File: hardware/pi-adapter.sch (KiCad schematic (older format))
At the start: 31 parts, among them P1 CONN_02X20, P10 CONN_01X04, P11 CONN_01X04, P12 CONN_01X04, P13 CONN_01X04, P14 CONN_01X04, P15 CONN_01X04, P16 CONN_01X04, P17 CONN_01X04, P18 CONN_01X04, P19 CONN_01X04, P2 +5V, P20 CONN_01X04, P21 CONN_01X04, P3 CONN_01X03, P4 GND, P5 CONN_01X03, P6 CONN_01X04, P7 CONN_01X04, P8 CONN_01X04, P9 CONN_01X04, U1 74HCT245, U2 74HCT245, U3 74HCT245, U4 74HCT245

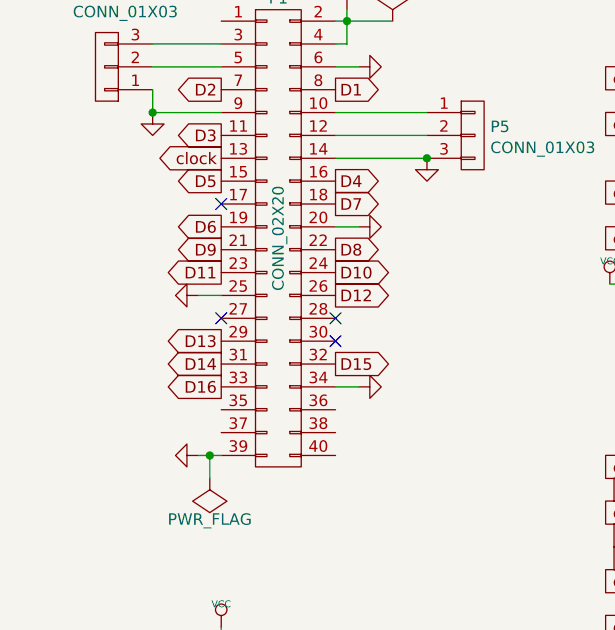
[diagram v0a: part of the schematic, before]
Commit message: o Break out SPI bus as well.
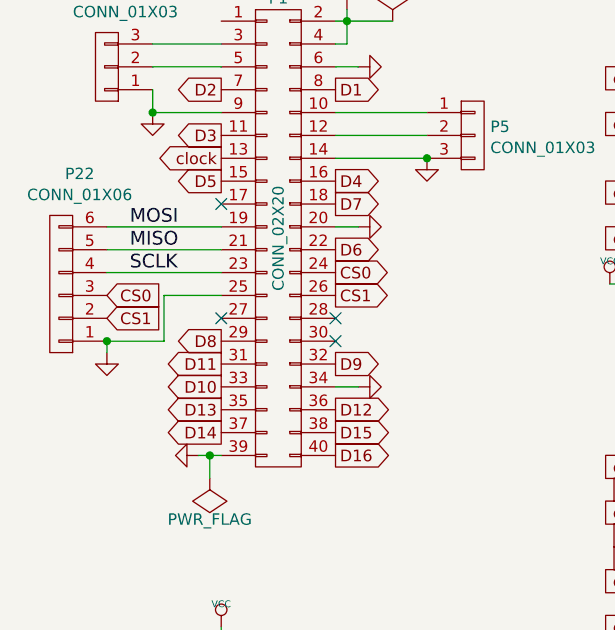
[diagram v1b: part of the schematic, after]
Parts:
- added P22: CONN_01X06, Pin_Headers:Pin_Header_Straight_1x06, symbol CONN_01X06
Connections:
- net D10: now also P1.33 (P33); no longer P1.24 (P24)
- net D11: now also P1.31 (P31); no longer P1.23 (P23)
- net D12: now also P1.36 (P36); no longer P1.26 (P26)
- net D13: now also P1.35 (P35); no longer P1.29 (P29)
- net D14: now also P1.37 (P37); no longer P1.31 (P31)
- net D15: now also P1.38 (P38); no longer P1.32 (P32)
- net D16: now also P1.40 (P40); no longer P1.33 (P33)
- net D6: now also P1.22 (P22); no longer P1.19 (P19)
- net D8: now also P1.29 (P29); no longer P1.22 (P22)
- net D9: now also P1.32 (P32); no longer P1.21 (P21)
- net GND: now also P22.1 (P1)
- new net CS0: P1.24 (P24), P22.3 (P3)
- new net CS1: P1.26 (P26), P22.2 (P2)
- new net MISO: P1.21 (P21), P22.5 (P5)
- new net MOSI: P1.19 (P19), P22.6 (P6)
- new net SCLK: P1.23 (P23), P22.4 (P4)
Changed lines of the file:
@@
 L GND #PWR05
 U 1 1 54ECB7BC
-P 1800 3900
-F 0 "#PWR05" H 1800 3900 30  0001 C CNN
-F 1 "GND" H 1800 3830 30  0001 C CNN
-F 2 "" H 1800 3900 60  0000 C CNN
-F 3 "" H 1800 3900 60  0000 C CNN
-	1    1800 3900
-	0    1    1    0
-$EndComp
-Wire Wire Line
-	1800 3900 1900 3900
+P 1400 4150
+F 0 "#PWR05" H 1400 4150 30  0001 C CNN
+F 1 "GND" H 1400 4080 30  0001 C CNN
+F 2 "" H 1400 4150 60  0000 C CNN
+F 3 "" H 1400 4150 60  0000 C CNN
+	1    1400 4150
+	1    0    0    -1
+$EndComp
+Wire Wire Line
+	1650 3900 1900 3900
 Text GLabel 1900 3000 0    51   Output ~ 0
 D2
-Text GLabel 2400 3700 2    51   Output ~ 0
+Text GLabel 1900 4100 0    51   Output ~ 0
 D8
-Text GLabel 1900 3700 0    51   Output ~ 0
+Text GLabel 2400 4200 2    51   Output ~ 0
 D9
-Text GLabel 2400 3800 2    51   Output ~ 0
+Text GLabel 1900 4300 0    51   Output ~ 0
 D10
-Text GLabel 1900 4100 0    51   Output ~ 0
+Text GLabel 1900 4400 0    51   Output ~ 0
 D13
 Text GLabel 1900 3300 0    51   Output ~ 0
 clock
+Text GLabel 1900 4500 0    51   Output ~ 0
+D14
+Text GLabel 2400 3700 2    51   Output ~ 0
+D6
+Text GLabel 2400 4600 2    51   Output ~ 0
+D16
+Text GLabel 2400 4500 2    51   Output ~ 0
+D15
+Text GLabel 2400 4400 2    51   Output ~ 0
+D12
 Text GLabel 1900 4200 0    51   Output ~ 0
-D14
-Text GLabel 1900 3600 0    51   Output ~ 0
-D6
-Text GLabel 1900 4300 0    51   Output ~ 0
-D16
-Text GLabel 2400 4200 2    51   Output ~ 0
-D15
-Text GLabel 2400 3900 2    51   Output ~ 0
-D12
-Text GLabel 1900 3800 0    51   Output ~ 0
 D11
 Text GLabel 1900 3400 0    51   Output ~ 0
@@
 Text Notes 5150 6100 0    60   ~ 0
 GND CLK DO +5V\n
+Wire Wire Line
+	1400 3600 1900 3600
+Wire Wire Line
+	1400 3700 1900 3700
+Wire Wire Line
+	1400 3800 1900 3800
+$Comp
+L CONN_01X06 P22
+U 1 1 56C265D6
+P 1200 3850
+F 0 "P22" H 1119 3368 50  0000 C CNN
+F 1 "CONN_01X06" H 1119 3460 50  0000 C CNN
+F 2 "Pin_Headers:Pin_Header_Straight_1x06" H 1119 3460 50  0001 C CNN
+F 3 "" H 1200 3850 50  0000 C CNN
+	1    1200 3850
+	-1   0    0    1
+$EndComp
+Wire Wire Line
+	1400 4100 1400 4150
+Wire Wire Line
+	1400 4100 1650 4100
+Wire Wire Line
+	1650 4100 1650 3900
+Text GLabel 2400 3800 2    51   Output ~ 0
+CS0
+Text GLabel 2400 3900 2    51   Output ~ 0
+CS1
+Text GLabel 1400 3900 2    51   Input ~ 0
+CS0
+Text GLabel 1400 4000 2    51   Input ~ 0
+CS1
+Connection ~ 1400 4100
+Text Label 1500 3600 0    60   ~ 0
+MOSI
+Text Label 1500 3700 0    60   ~ 0
+MISO
+Text Label 1500 3800 0    60   ~ 0
+SCLK
 $EndSCHEMATC

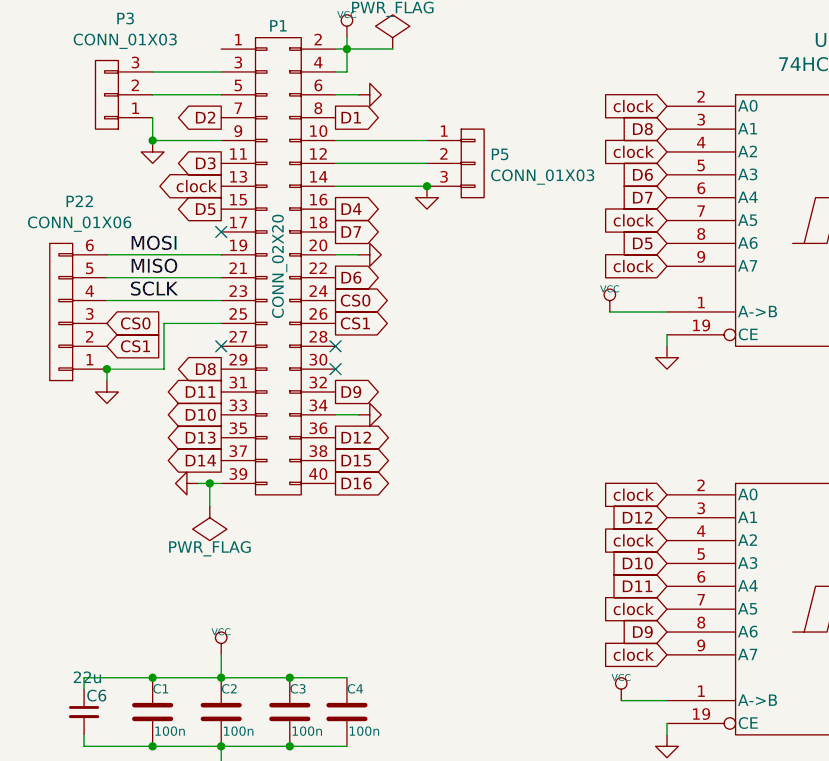
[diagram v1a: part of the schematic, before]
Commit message: o Better sequential labelling of data lines. o Improve higher current traces.
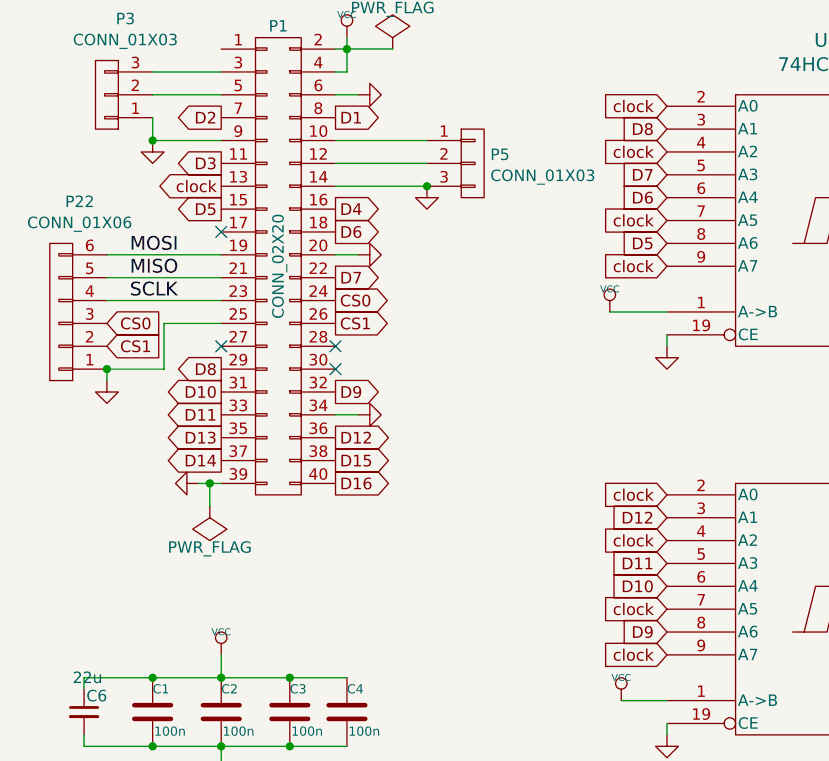
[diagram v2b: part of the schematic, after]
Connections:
- net D10: now also P1.31 (P31), U3.6 (A4); no longer P1.33 (P33), U3.5 (A3)
- net D11: now also P1.33 (P33), U3.5 (A3); no longer P1.31 (P31), U3.6 (A4)
- net D6: now also P1.18 (P18), U2.6 (A4); no longer P1.22 (P22), U2.5 (A3)
- net D7: now also P1.22 (P22), U2.5 (A3); no longer P1.18 (P18), U2.6 (A4)
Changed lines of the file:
@@
 Text GLabel 2400 4200 2    51   Output ~ 0
 D9
-Text GLabel 1900 4300 0    51   Output ~ 0
+Text GLabel 1900 4200 0    51   Output ~ 0
 D10
 Text GLabel 1900 4400 0    51   Output ~ 0
@@
 Text GLabel 1900 4500 0    51   Output ~ 0
 D14
-Text GLabel 2400 3700 2    51   Output ~ 0
+Text GLabel 2400 3500 2    51   Output ~ 0
 D6
 Text GLabel 2400 4600 2    51   Output ~ 0
@@
 Text GLabel 2400 4400 2    51   Output ~ 0
 D12
-Text GLabel 1900 4200 0    51   Output ~ 0
+Text GLabel 1900 4300 0    51   Output ~ 0
 D11
 Text GLabel 1900 3400 0    51   Output ~ 0
@@
 	1600 3100 1600 3000
 Connection ~ 1600 3100
-Text GLabel 2400 3500 2    51   Output ~ 0
+Text GLabel 2400 3700 2    51   Output ~ 0
 D7
 Text GLabel 3850 1850 0    51   Input ~ 0
@@
 Text GLabel 3850 3550 0    51   Input ~ 0
 D5
+Text GLabel 3850 3350 0    51   Input ~ 0
+D6
 Text GLabel 3850 3250 0    51   Input ~ 0
-D6
-Text GLabel 3850 3350 0    51   Input ~ 0
 D7
 Text GLabel 3850 3050 0    51   Input ~ 0
@@
 Text GLabel 3850 5250 0    51   Input ~ 0
 D9
+Text GLabel 3850 5050 0    51   Input ~ 0
+D10
 Text GLabel 3850 4950 0    51   Input ~ 0
-D10
-Text GLabel 3850 5050 0    51   Input ~ 0
 D11
 Text GLabel 3850 4750 0    51   Input ~ 0

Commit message: o Less vias where text is. o Moar copper.
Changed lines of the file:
@@
 	2450 2650 2450 2800
-Wire Wire Line
-	2400 2700 2650 2700
 Wire Wire Line
 	2450 2800 2400 2800
@@
 NoConn ~ 1900 3500
 $Comp
-L PWR_FLAG #FLG016
-U 1 1 557B1FD6
-P 2650 2700
-F 0 "#FLG016" H 2650 2795 50  0001 C CNN
-F 1 "PWR_FLAG" H 2650 2880 50  0000 C CNN
-F 2 "" H 2650 2700 60  0000 C CNN
-F 3 "" H 2650 2700 60  0000 C CNN
-	1    2650 2700
-	1    0    0    -1
-$EndComp
-$Comp
 L PWR_FLAG #FLG017
 U 1 1 557B23A7
@@
 L VCC #PWR019
 U 1 1 562B12CC
-P 1950 1600
-F 0 "#PWR019" H 1950 1700 30  0001 C CNN
-F 1 "VCC" H 1950 1700 30  0000 C CNN
-F 2 "" H 1950 1600 60  0000 C CNN
-F 3 "" H 1950 1600 60  0000 C CNN
-	1    1950 1600
+P 1950 1400
+F 0 "#PWR019" H 1950 1500 30  0001 C CNN
+F 1 "VCC" H 1950 1500 30  0000 C CNN
+F 2 "" H 1950 1400 60  0000 C CNN
+F 3 "" H 1950 1400 60  0000 C CNN
+	1    1950 1400
 	1    0    0    -1
 $EndComp
@@
 Text Label 1500 3800 0    60   ~ 0
 SCLK
+$Comp
+L PWR_FLAG #FLG?
+U 1 1 56CA81D8
+P 2550 1600
+F 0 "#FLG?" H 2550 1695 50  0001 C CNN
+F 1 "PWR_FLAG" V 2550 1950 50  0000 C CNN
+F 2 "" H 2550 1600 60  0000 C CNN
+F 3 "" H 2550 1600 60  0000 C CNN
+	1    2550 1600
+	1    0    0    -1
+$EndComp
+Connection ~ 2550 1600
+Wire Wire Line
+	1950 1400 1950 1600
+$Comp
+L PWR_FLAG #FLG?
+U 1 1 56CA8545
+P 1950 1450
+F 0 "#FLG?" H 1950 1545 50  0001 C CNN
+F 1 "PWR_FLAG" V 1950 1800 50  0000 C CNN
+F 2 "" H 1950 1450 60  0000 C CNN
+F 3 "" H 1950 1450 60  0000 C CNN
+	1    1950 1450
+	0    -1   -1   0
+$EndComp
+Connection ~ 1950 1450
+Wire Wire Line
+	2400 2700 2450 2700
 $EndSCHEMATC

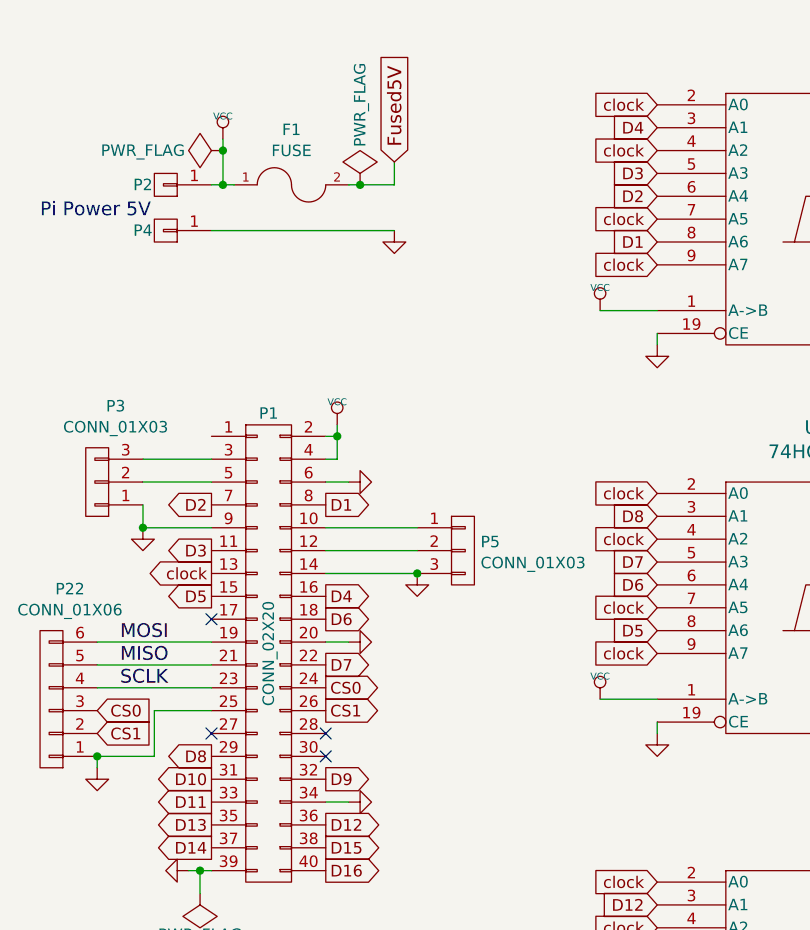
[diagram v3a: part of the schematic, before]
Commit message: o Doh': serial interface connection was off by one pin.
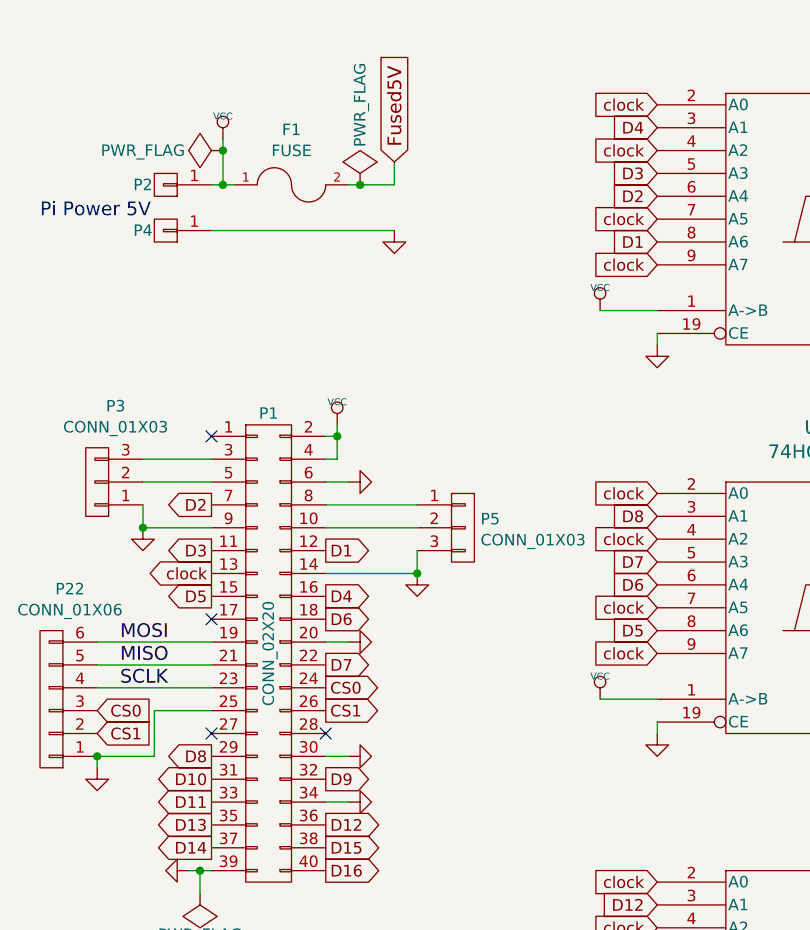
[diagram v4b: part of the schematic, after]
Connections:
- net D1: now also P1.12 (P12); no longer P1.8 (P8)
- net GND: now also P1.30 (P30)
- net at P1.10 (P10): now also P5.2 (P2); no longer P5.1 (P1)
- new net: P1.8 (P8), P5.1 (P1)
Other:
- moved on the sheet: P5
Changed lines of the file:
@@
 Text GLabel 2400 3400 2    51   Output ~ 0
 D4
-Text GLabel 2400 3000 2    51   Output ~ 0
+Text GLabel 2400 3200 2    51   Output ~ 0
 D1
 $Comp
@@
 NoConn ~ 1900 4000
 NoConn ~ 2400 4000
-NoConn ~ 2400 4100
 NoConn ~ 1900 3500
 $Comp
@@
 L CONN_01X03 P5
 U 1 1 56C196A7
-P 3000 3200
-F 0 "P5" H 3077 3238 50  0000 L CNN
-F 1 "CONN_01X03" H 3077 3146 50  0000 L CNN
-F 2 "Pin_Headers:Pin_Header_Straight_1x03" H 3000 3200 50  0001 C CNN
-F 3 "" H 3000 3200 50  0000 C CNN
-	1    3000 3200
-	1    0    0    -1
-$EndComp
-Wire Wire Line
-	2400 3100 2800 3100
-Wire Wire Line
-	2400 3200 2800 3200
+P 3000 3100
+F 0 "P5" H 3077 3138 50  0000 L CNN
+F 1 "CONN_01X03" H 3077 3046 50  0000 L CNN
+F 2 "Pin_Headers:Pin_Header_Straight_1x03" H 3000 3100 50  0001 C CNN
+F 3 "" H 3000 3100 50  0000 C CNN
+	1    3000 3100
+	1    0    0    -1
+$EndComp
 $Comp
 L GND #PWR021
@@
 	1    0    0    -1
 $EndComp
-Wire Wire Line
-	2400 3300 2800 3300
-Connection ~ 2800 3300
 $Comp
 L CONN_01X03 P3
@@
 Fused5V
 Wire Wire Line
-	2700 1500 2700 1600
+	2700 1600 2700 1500
 Text GLabel 6250 1600 2    60   Input ~ 0
 Fused5V
@@
 Connection ~ 1600 5750
 Wire Wire Line
-	2700 1600 2500 1600
+	2500 1600 2700 1600
 Wire Wire Line
 	1900 1800 2700 1800
@@
 Wire Wire Line
 	2400 2700 2450 2700
+$Comp
+L GND #PWR?
+U 1 1 56CF0349
+P 2500 4100
+F 0 "#PWR?" H 2500 4100 30  0001 C CNN
+F 1 "GND" H 2500 4030 30  0001 C CNN
+F 2 "" H 2500 4100 60  0000 C CNN
+F 3 "" H 2500 4100 60  0000 C CNN
+	1    2500 4100
+	0    -1   -1   0
+$EndComp
+Wire Wire Line
+	2400 4100 2500 4100
+NoConn ~ 1900 2700
+Wire Wire Line
+	2800 3200 2800 3300
+Wire Wire Line
+	2800 3300 2400 3300
+Connection ~ 2800 3300
+Wire Wire Line
+	2400 3000 2800 3000
+Wire Wire Line
+	2400 3100 2800 3100
 $EndSCHEMATC

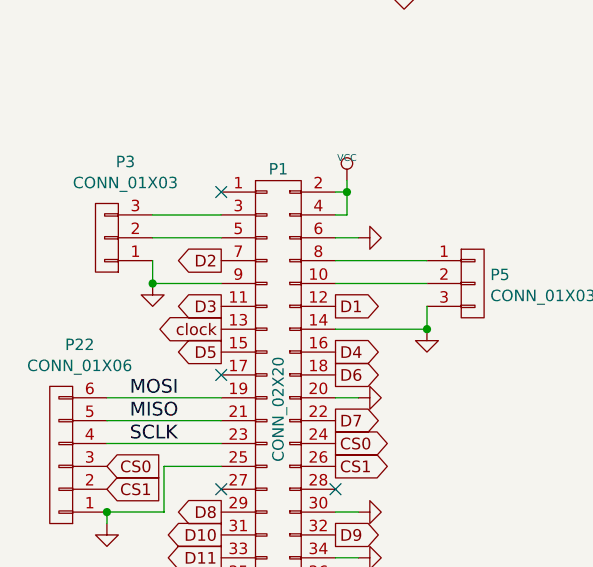
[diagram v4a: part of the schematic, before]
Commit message: o Add thermal reliefs for GND. o Add rounded corners.
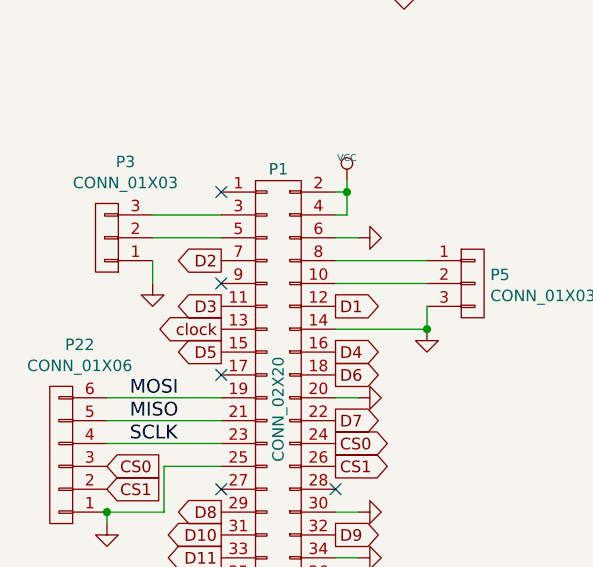
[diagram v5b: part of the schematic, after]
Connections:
- net GND: no longer P1.9 (P9)
- no-connect marks 4 -> 5
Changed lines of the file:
@@
 	1    0    0    -1
 $EndComp
-Wire Wire Line
-	1900 3100 1600 3100
-Wire Wire Line
-	1600 3100 1600 3000
-Connection ~ 1600 3100
 Text GLabel 2400 3700 2    51   Output ~ 0
 D7
@@
 Wire Wire Line
 	2400 3100 2800 3100
+Wire Wire Line
+	1600 3100 1600 3000
+NoConn ~ 1900 3100
 $EndSCHEMATC
